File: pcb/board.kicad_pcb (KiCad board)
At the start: 4 copper layers, 159.9 x 99.9 mm, 168 parts, among them J1 Conn_02x03_Counter_Clockwise, J2 USB_B, J3 650913-5, SW1 SW_Push, U1 XC6SLX16-FTG256, U10 TPS541620, U11 74LVC1G08, U12 IS42S16100H, U13 IS42S16100H, U14 ECS-7050MV, U15 BCM56DS, U16 74LVC1G32, U17 74LS04, U18 74LS08, U19 LMC555xMM, U2 74LVC157, U3 AT25xxx, U4 TMUX1219, U5 AT25xxx, U6 74LVC1G04, U7 SN74AVC4T245PW, U8 FT2232HQ, U9 93LCxxBxxOT, Y1 12MHz

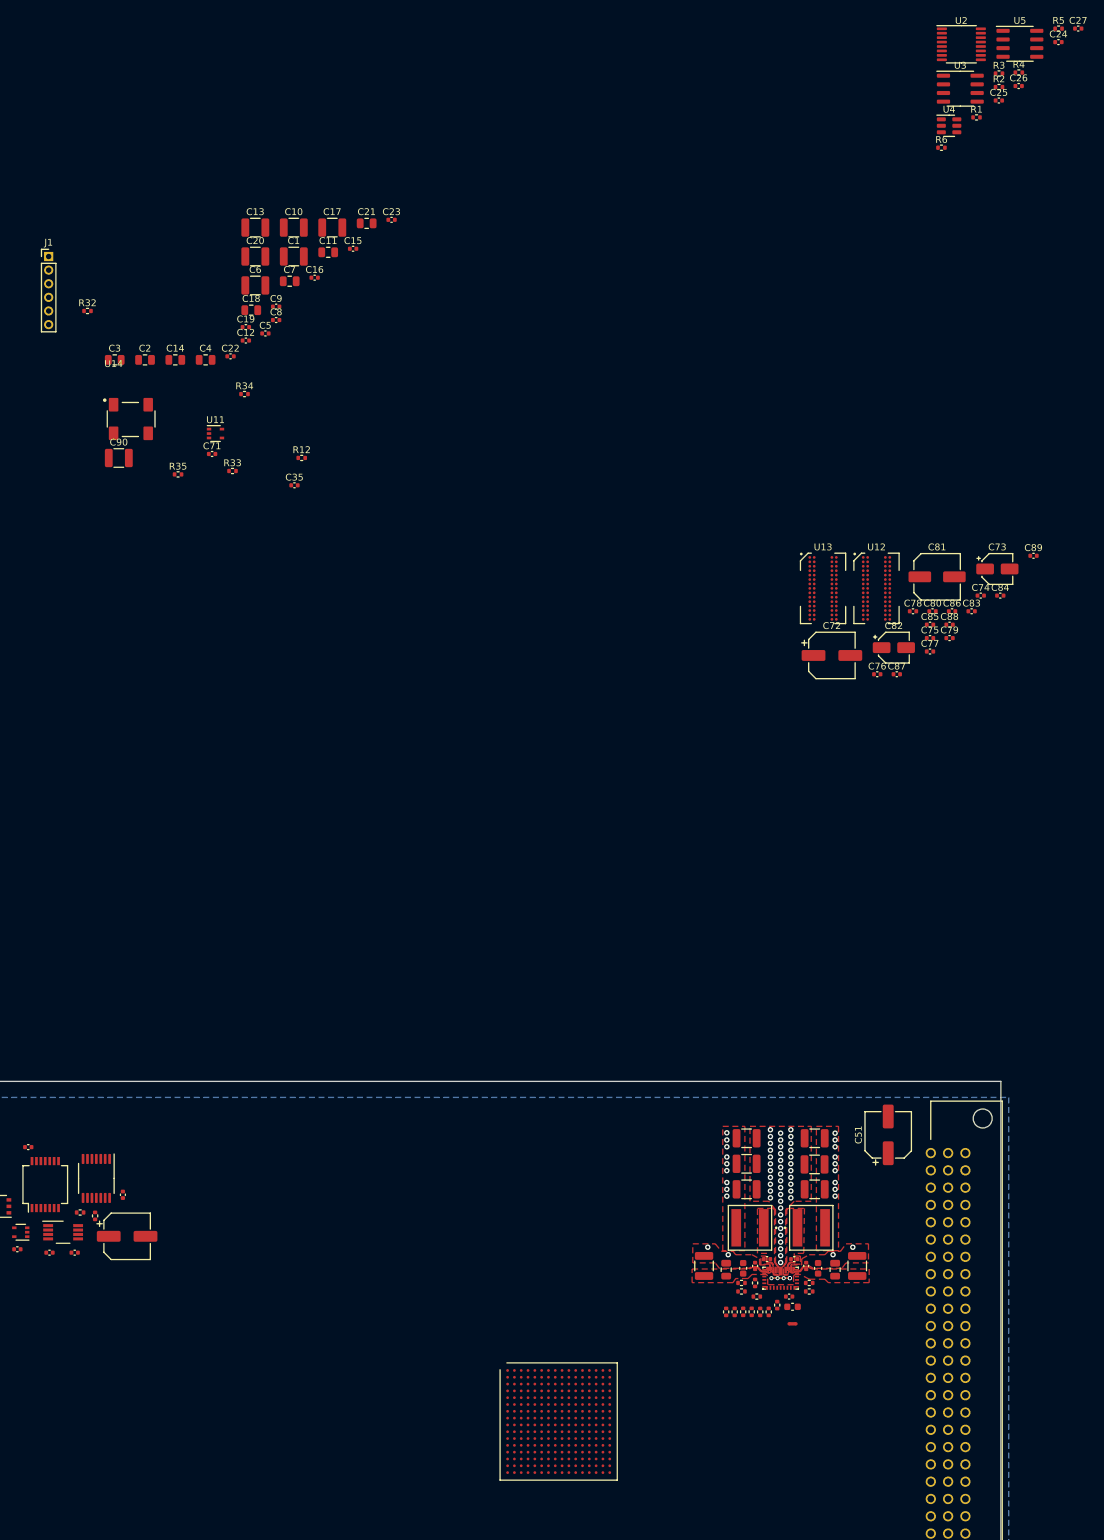
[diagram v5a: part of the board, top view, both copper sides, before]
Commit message: route pol
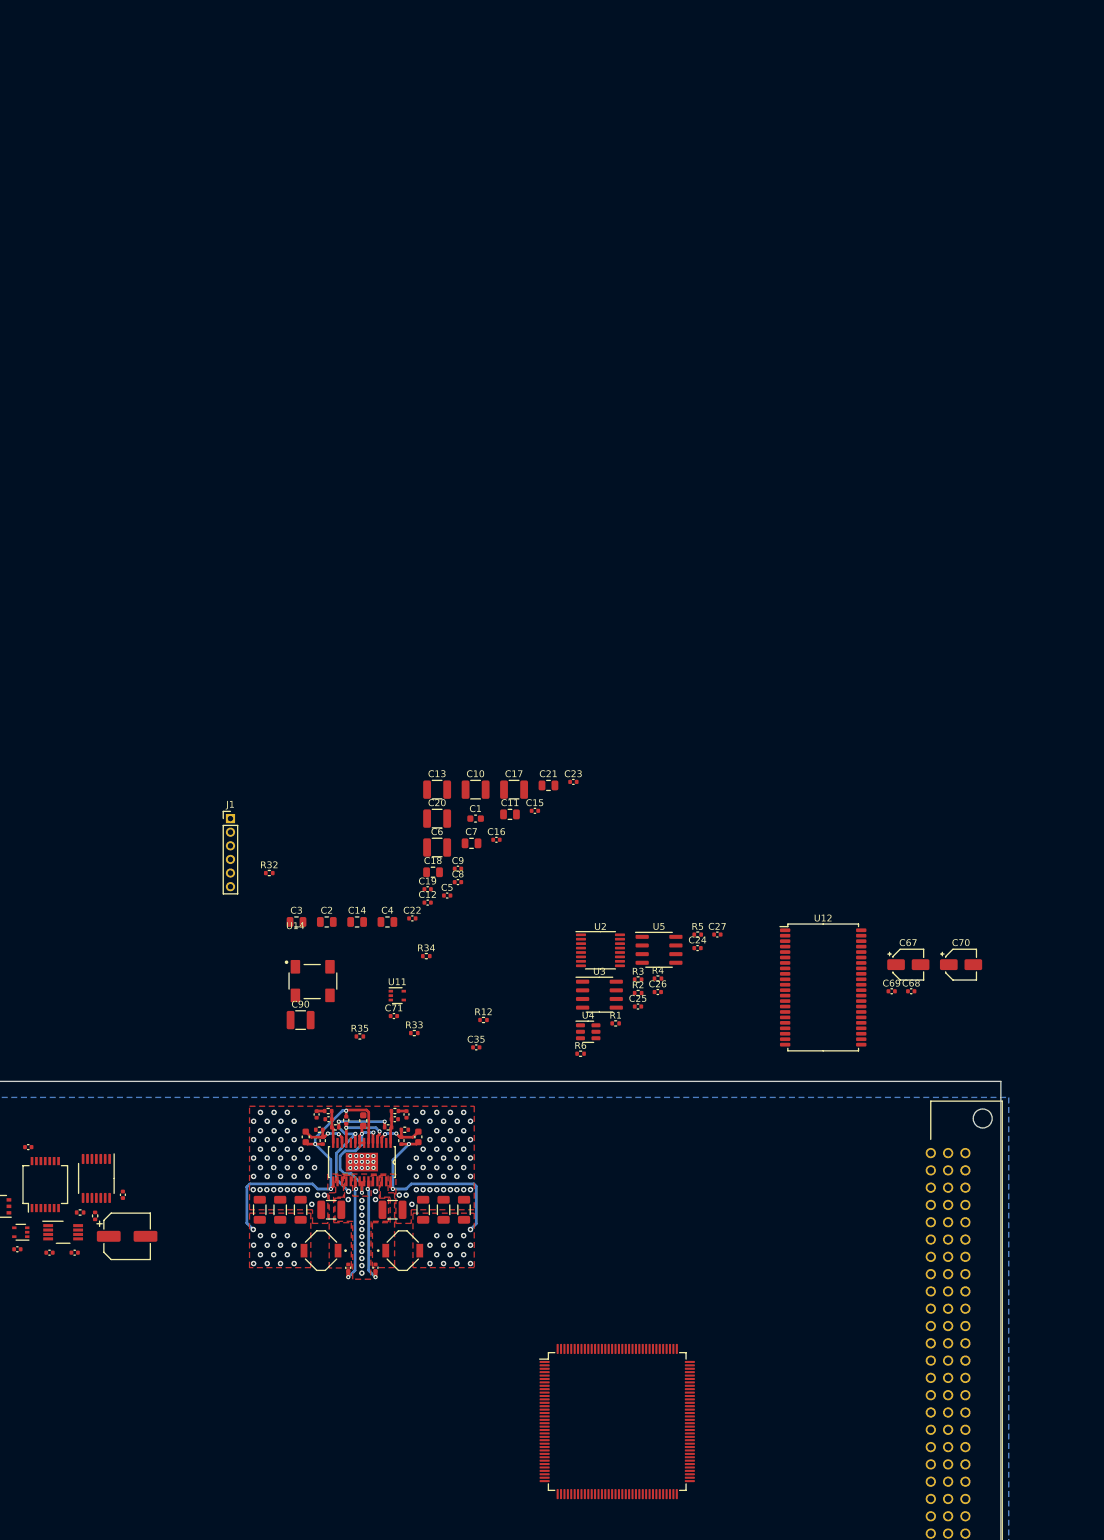
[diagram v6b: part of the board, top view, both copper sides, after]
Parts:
- removed C72: 100uF, Capacitor_SMD:CP_Elec_6.3x7.7
- removed C73, C82: 4.7uF, Capacitor_SMD:CP_Elec_4x4.5
- removed C74, C75, C76, C77, C78, C79, C80, C83, C84, C85, C86, C87, C88, C89: 470nF, Capacitor_SMD:C_0402_1005Metric
- removed C81: 100uF, Capacitor_SMD:C_Elec_6.3x7.7
- removed NT1: NetTie_2, NetTie:NetTie-2_SMD_Pad0.5mm
- removed R28: 8k, Resistor_SMD:R_0402_1005Metric
- removed R29: 39.9k, Resistor_SMD:R_0402_1005Metric
- removed R30: 15.4k, Resistor_SMD:R_0402_1005Metric
- removed R31: 17.4k, Resistor_SMD:R_0402_1005Metric
- removed U13: IS42S16100H, IS42S16100H:IS42S16100H
- added C64: 22u, Capacitor_SMD:C_1206_3216Metric, F.Cu at (109.1, 63.9)
- added C68: 0.1u, Capacitor_SMD:C_0402_1005Metric, F.Cu at (201.8, 31.8)
- C1: footprint Capacitor_SMD:C_1210_3225Metric -> Capacitor_SMD:C_0603_1608Metric
- C47: value 100uF -> 47u
- C51: value 100uF -> 47u; footprint Capacitor_SMD:CP_Elec_6.3x7.7 -> Capacitor_SMD:C_1210_3225Metric
- C52: value 47uF -> 100n; footprint Capacitor_SMD:C_1210_3225Metric -> Capacitor_SMD:C_0402_1005Metric
- C53: value 22uF -> NL; footprint Capacitor_SMD:C_0805_2012Metric -> Capacitor_SMD:C_0603_1608Metric
- C54: value 0.1uF -> 22u; footprint Capacitor_SMD:C_0603_1608Metric -> Capacitor_SMD:C_1206_3216Metric
- C55, C63: value 0.1uF -> 22u; footprint Capacitor_SMD:C_0402_1005Metric -> Capacitor_SMD:C_1206_3216Metric
- C56: value 0.1uF -> 10u; footprint Capacitor_SMD:C_0402_1005Metric -> Capacitor_SMD:C_1206_3216Metric
- C57: value 100uF -> 100n; footprint Capacitor_SMD:C_1210_3225Metric -> Capacitor_SMD:C_0402_1005Metric
- C58: value 100uF -> 10p; footprint Capacitor_SMD:C_1210_3225Metric -> Capacitor_SMD:C_0402_1005Metric
- C59: value 100uF -> 220p; footprint Capacitor_SMD:C_1210_3225Metric -> Capacitor_SMD:C_0402_1005Metric
- C60: value 47uF -> 10p; footprint Capacitor_SMD:C_1210_3225Metric -> Capacitor_SMD:C_0402_1005Metric
- C61: value 22uF -> 220p; footprint Capacitor_SMD:C_0805_2012Metric -> Capacitor_SMD:C_0402_1005Metric
- C62: value 0.1uF -> NL
- C65: value 4.7uF -> 10u; footprint Capacitor_SMD:C_0603_1608Metric -> Capacitor_SMD:C_1206_3216Metric
- C66: value 0.1uF -> 2.2uF; footprint Capacitor_SMD:C_0402_1005Metric -> Capacitor_SMD:C_0603_1608Metric
- C67: value 0.1uF -> 4.7u; footprint Capacitor_SMD:C_0402_1005Metric -> Capacitor_SMD:CP_Elec_4x4.5
- C69: value 100uF -> 0.1u; footprint Capacitor_SMD:C_1210_3225Metric -> Capacitor_SMD:C_0402_1005Metric
- C70: value 100uF -> 4.7u; footprint Capacitor_SMD:C_1210_3225Metric -> Capacitor_SMD:CP_Elec_4x4.5
- L1: value 560nH -> 1uH; footprint XAL6030-561MEB:IND_XAL6030-561MEB -> 2020_5252_Inductor:IND_#A915BY-100M=P3
- L2: value 1.2uH -> 2.2uH; footprint XAL6030-122MEB:IND_XAL6030-122MEB -> 2020_5252_Inductor:IND_#A915BY-100M=P3
- R19: value 100k -> 10k
- R20: value 14k -> 10k
- R23: value 10k -> 6.98k
- R24: value 100k -> 6.98k
- R25: value 56k -> 10k
- R26: value 10k -> 45.3k
- U1: value XC6SLX16-FTG256 -> XC6SLX9-TQG144; footprint Package_BGA:Xilinx_FTG256 -> Package_QFP:TQFP-144_20x20mm_P0.5mm
- U10: value TPS541620 -> LTC3633EFEPBF; footprint TPS541620:TPS541620 -> SOP65P640X120-29N:SOP65P640X120-29N
- U12: value IS42S16100H -> IS61WV25616EFBLL; footprint IS42S16100H:IS42S16100H -> Package_SO:TSOP-II-44_10.16x18.41mm_P0.8mm
- moved C24 143.2 mm to (170.4, 25.5)
- moved C25 143.2 mm to (161.6, 34.1)
- moved C26 143.2 mm to (164.5, 31.9)
- moved C27 143.2 mm to (173.3, 23.5)
- moved R1 143.2 mm to (158.3, 36.6)
- moved R2 143.2 mm to (161.7, 32.1)
- moved R3 143.2 mm to (161.7, 30.1)
- moved R4 143.2 mm to (164.6, 30.0)
- moved R5 143.2 mm to (170.4, 23.5)
- moved R6 143.2 mm to (153.2, 41.0)
- moved U2 143.2 mm to (156.1, 25.8)
- moved U3 143.2 mm to (156.0, 32.3)
- moved U4 143.2 mm to (154.3, 37.8)
- moved U5 143.2 mm to (164.7, 25.8)
- moved C19 86.8 mm to (130.7, 16.9)
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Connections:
- C47 pad 1: VCCAUX -> +5V
- C51 pad 1: VCC -> +5V
- C52 pad 1: VCC -> Net-(U10-Pad23)
- C52 pad 2: GND -> Net-(L1-Pad1)
- C53 pad 1: VCC -> VCCINT
- C53 pad 2: GND -> Net-(C53-Pad2)
- C54 pad 1: VCC -> VCCINT
- C55 pad 1: VCC -> VCCINT
- C56 pad 1: Net-(C56-Pad1) -> VCCINT
- C56 pad 2: Net-(C56-Pad2) -> GND
- C57 pad 1: VCCINT -> Net-(C57-Pad1)
- C57 pad 2: GND -> Net-(C57-Pad2)
- C58 pad 1: VCCINT -> Net-(C58-Pad1)
- C59 pad 1: VCCINT -> Net-(C59-Pad1)
- C60 pad 1: VCC -> Net-(C60-Pad1)
- C61 pad 1: VCC -> Net-(C61-Pad1)
- C62 pad 1: VCC -> VCCAUX
- C62 pad 2: GND -> Net-(C62-Pad2)
- C63 pad 1: VCC -> VCCAUX
- C65 pad 1: /Power Supply/BP5 -> VCCAUX
- C66 pad 1: /Power Supply/BP5 -> Net-(C66-Pad1)
- C67 pad 1: Net-(C67-Pad1) -> VCCAUX
- C67 pad 2: Net-(C67-Pad2) -> GND
- J3 pad 19: VCC -> +5V
- J3 pad 6: VCC -> +5V
- J3 pad 76: VCC -> +5V
- J3 pad 89: VCC -> +5V
- L1 pad 1: Net-(C56-Pad2) -> Net-(L1-Pad1)
- L2 pad 1: Net-(C67-Pad2) -> Net-(C57-Pad2)
- R19 pad 1: Net-(R19-Pad1) -> +5V
- R19 pad 2: /Power Supply/BP5 -> Net-(C58-Pad1)
- R20 pad 1: Net-(C64-Pad1) -> +5V
- R20 pad 2: VCCINT -> Net-(C60-Pad1)
- R21 pad 1: GND1 -> VCCAUX
- R21 pad 2: Net-(C64-Pad1) -> Net-(R21-Pad2)
- R22 pad 1: VCCAUX -> VCCINT
- R22 pad 2: /Power Supply/EN1 -> Net-(C53-Pad2)
- R23 pad 1: VCC -> Net-(C58-Pad1)
- R23 pad 2: /Power Supply/EN2 -> Net-(C59-Pad1)
- R24 pad 1: Net-(R24-Pad1) -> Net-(C60-Pad1)
- R24 pad 2: /Power Supply/BP5 -> Net-(C61-Pad1)
- R25 pad 1: Net-(C68-Pad1) -> Net-(C53-Pad2)
- R25 pad 2: VCCAUX -> GND
- R26 pad 1: Net-(R26-Pad1) -> VCCAUX
- R26 pad 2: Net-(R26-Pad2) -> Net-(C62-Pad2)
- R27 pad 1: GND1 -> Net-(C62-Pad2)
- R27 pad 2: Net-(C68-Pad1) -> GND
- U10 pad 1: Net-(C67-Pad1) -> Net-(C60-Pad1)
- U10 pad 10: Net-(R26-Pad2) -> GND
- U10 pad 11: (no net) -> Net-(R21-Pad2)
- U10 pad 12: /Power Supply/SS -> Net-(C62-Pad2)
- U10 pad 13: Net-(C64-Pad1) -> unconnected-(U10-Pad13)
- U10 pad 14: GND -> Net-(C58-Pad1)
- U10 pad 15: GND1 -> VCCAUX
- U10 pad 16: /Power Supply/BP5 -> Net-(C57-Pad2)
- U10 pad 17: Net-(C68-Pad1) -> Net-(C57-Pad2)
- U10 pad 18: /Power Supply/EN2 -> +5V
- U10 pad 19: (no net) -> +5V
- U10 pad 2: Net-(C67-Pad2) -> unconnected-(U10-Pad2)
- U10 pad 20: /Power Supply/EN1 -> Net-(C57-Pad1)
- U10 pad 21: Net-(R24-Pad1) -> Net-(C66-Pad1)
- U10 pad 22: Net-(R19-Pad1) -> Net-(C66-Pad1)
- U10 pad 23: GND -> Net-(U10-Pad23)
- U10 pad 24: VCC -> +5V
- U10 pad 25: GND -> +5V
- U10 pad 3: GND -> Net-(C53-Pad2)
- U10 pad 4: Net-(C56-Pad2) -> Net-(R21-Pad2)
- U10 pad 5: Net-(C56-Pad1) -> Net-(C66-Pad1)
- U10 pad 6: VCC -> VCCAUX
- U10 pad 7: GND -> Net-(C66-Pad1)
- U10 pad 8: /Power Supply/SYNC -> Net-(C66-Pad1)
- U10 pad 9: Net-(R26-Pad1) -> +5V
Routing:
- net VCCAUX: track 0.00 -> 46.9 mm, vias 9 -> 18
- net VCCINT: track 0.00 -> 30.9 mm, vias 9 -> 17
- net +5V: track 0.00 -> 23.8 mm, vias 0 -> 18
- net Net-(C66-Pad1): track 0.00 -> 21.8 mm, vias 0 -> 3
- net Net-(C57-Pad1): track 0.00 -> 15.5 mm, vias 0 -> 2
- net Net-(U10-Pad23): track 0.00 -> 15.5 mm, vias 0 -> 2
- net Net-(R21-Pad2): track 0.00 -> 9.76 mm, vias 0 -> 2
- net Net-(C53-Pad2): track 0.00 -> 8.08 mm, vias 0 -> 2
- net Net-(C62-Pad2): track 0.00 -> 8.03 mm, vias 0 -> 2
- net Net-(C58-Pad1): track 0.00 -> 4.77 mm
- net Net-(C60-Pad1): track 0.00 -> 4.75 mm
- net Net-(C61-Pad1): track 0.00 -> 1.20 mm
- net Net-(C59-Pad1): track 0.00 -> 1.20 mm
- net VCC: vias 4 -> 0
- net GND: vias 47 -> 107
- added copper zone on F.Cu, net +5V
- added copper zone on In2.Cu, net +5V
- added copper zone on F.Cu, net Net-(C57-Pad2)
- added copper zone on F.Cu, net Net-(L1-Pad1)
- added copper zone on In2.Cu, net VCCAUX
- added copper zone on In2.Cu, net VCCINT
- removed copper zone on F.Cu, net Net-(C56-Pad1)
- removed copper zone on F.Cu, net Net-(C56-Pad2)
- removed copper zone on F.Cu, net Net-(C67-Pad1)
- removed copper zone on F.Cu, net Net-(C67-Pad2)
- removed copper zone on F.Cu, net VCC

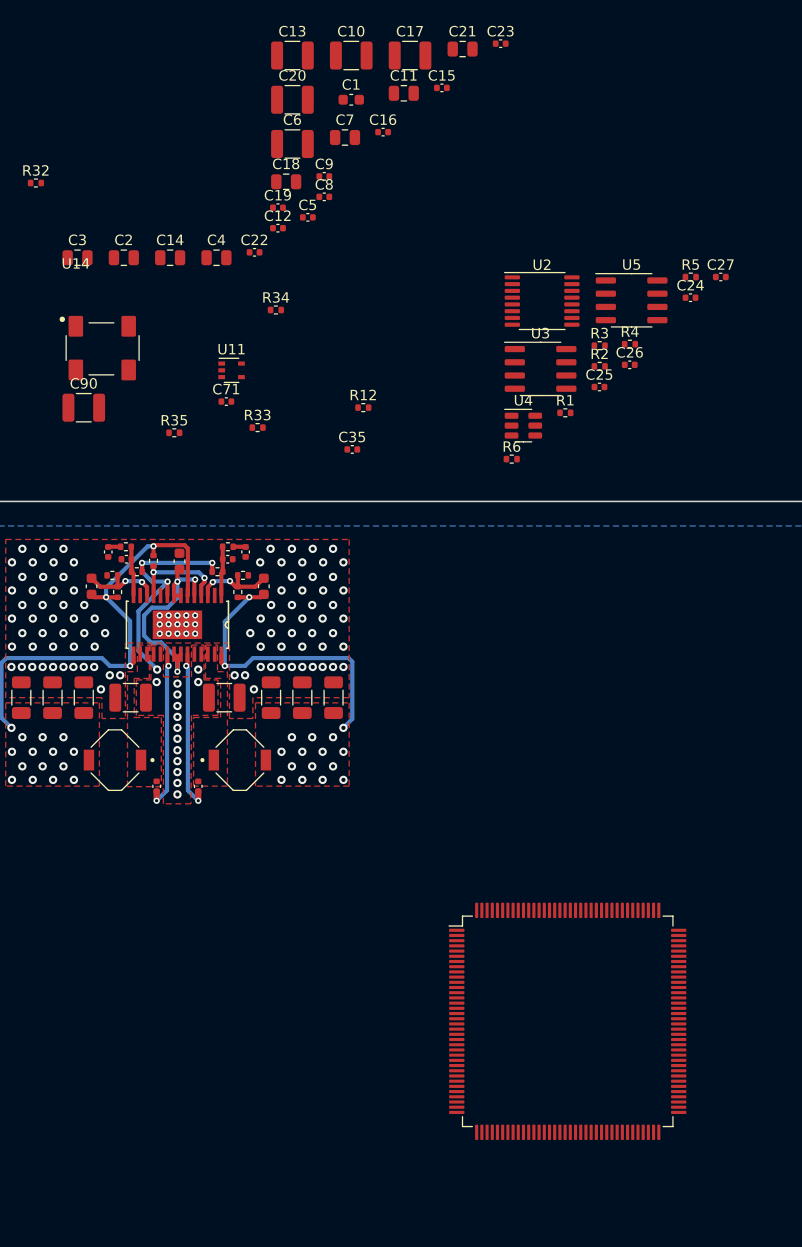
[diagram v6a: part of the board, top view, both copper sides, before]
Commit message: add decoupling caps
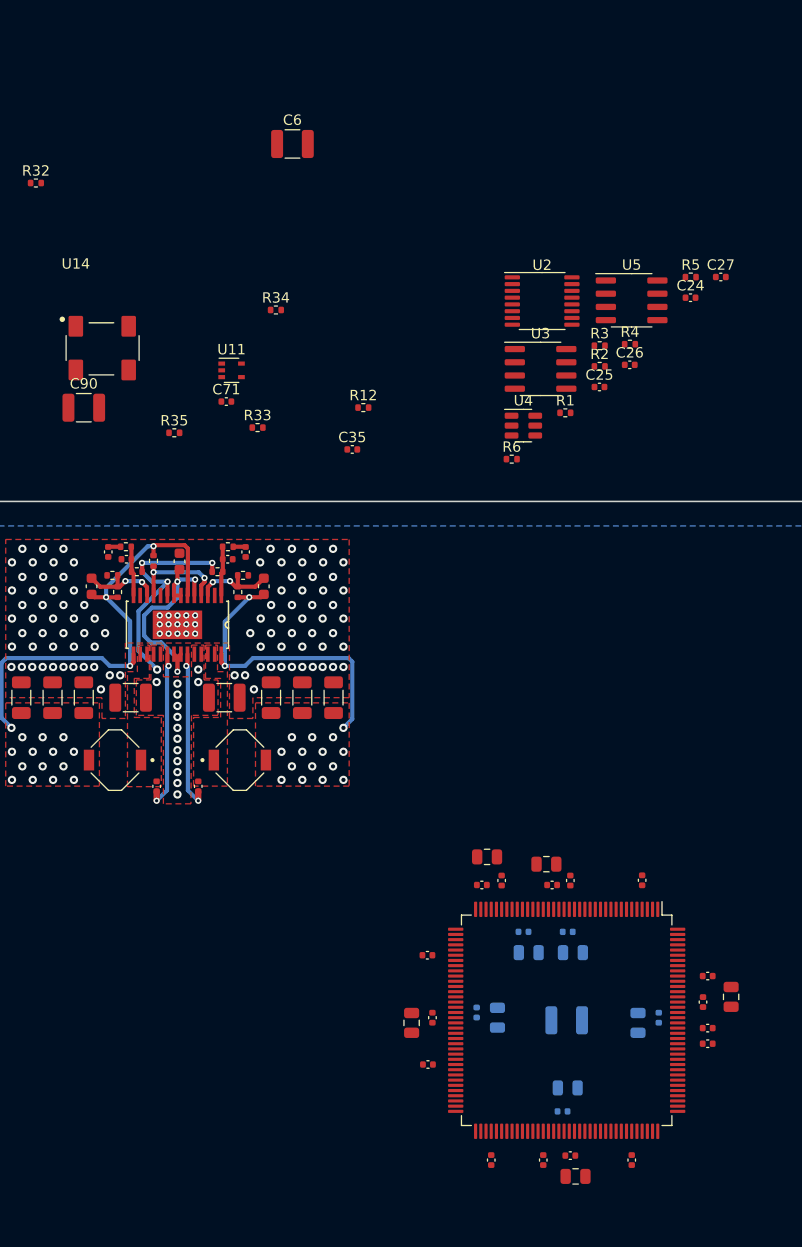
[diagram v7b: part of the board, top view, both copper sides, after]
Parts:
- removed C20: 100uF, Capacitor_SMD:C_1210_3225Metric
- removed C21: 4.7uF, Capacitor_SMD:C_0805_2012Metric
- removed C23: 470nF, Capacitor_SMD:C_0402_1005Metric
- added C72: 4.7uF, Capacitor_SMD:C_0805_2012Metric, B.Cu at (151.8, 94.7)
- added C73: 4.7uF, Capacitor_SMD:C_0805_2012Metric, B.Cu at (154.8, 88.4)
- added C74: 470nF, Capacitor_SMD:C_0402_1005Metric, B.Cu at (158.1, 103.7)
- added C75: 470nF, Capacitor_SMD:C_0402_1005Metric, B.Cu at (167.3, 94.7)
- added C76: 470nF, Capacitor_SMD:C_0402_1005Metric, B.Cu at (149.8, 94.2)
- added C77: 470nF, Capacitor_SMD:C_0402_1005Metric, B.Cu at (154.3, 86.4)
- added C78: 4.7uF, Capacitor_SMD:C_0805_2012Metric, F.Cu at (156.5, 79.9)
- added C79: 4.7uF, Capacitor_SMD:C_0805_2012Metric, F.Cu at (143.6, 95.2)
- added C80: 4.7uF, Capacitor_SMD:C_0805_2012Metric, F.Cu at (159.3, 109.9)
- added C81: 4.7uF, Capacitor_SMD:C_0805_2012Metric, F.Cu at (150.8, 79.2)
- added C82: 470nF, Capacitor_SMD:C_0402_1005Metric, F.Cu at (171.6, 93.2)
- added C83: 470nF, Capacitor_SMD:C_0402_1005Metric, F.Cu at (158.8, 107.9)
- added C84: 470nF, Capacitor_SMD:C_0402_1005Metric, F.Cu at (145.6, 94.7)
- C1: footprint Capacitor_SMD:C_0603_1608Metric -> Capacitor_SMD:C_1210_3225Metric; moved to B.Cu
- C10, C13, C17: value 100uF -> 470nF; footprint Capacitor_SMD:C_1210_3225Metric -> Capacitor_SMD:C_0402_1005Metric
- C11, C14, C18: value 4.7uF -> 470nF; footprint Capacitor_SMD:C_0805_2012Metric -> Capacitor_SMD:C_0402_1005Metric
- C2, C3, C4, C5: moved to B.Cu
- moved C13 107.8 mm to (151.2, 108.4), turned to -90 degrees
- moved C15 103.5 mm to (156.2, 108.4), turned to -90 degrees
- moved C16 101.6 mm to (164.7, 108.4), turned to -90 degrees
- moved C10 100.9 mm to (172.0, 97.2)
- moved C17 97.0 mm to (145.2, 99.2), turned to 180 degrees
- moved C3 91.1 mm to (165.3, 95.2), turned to -90 degrees
- moved C1 90.8 mm to (158.5, 94.9)
- moved C7 90.5 mm to (174.3, 92.7), turned to 90 degrees
- moved C11 89.7 mm to (172.0, 90.7)
- moved C12 87.2 mm to (172.0, 95.7)
- moved C4 86.6 mm to (158.6, 101.4)
- moved C2 79.5 mm to (159.1, 88.4)
- moved C18 75.3 mm to (165.7, 81.5), turned to 90 degrees
- moved C5 73.1 mm to (158.6, 86.4)
- moved C14 71.4 mm to (145.1, 88.7), turned to 180 degrees
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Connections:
- U1 pad 128: unconnected-(U1-Pad128) -> VCCINT
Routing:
- net Net-(C52-Pad1): vias 2 -> 1
- net (no net): vias 0 -> 1

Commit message: place all components
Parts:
- moved J1 133.5 mm to (104.1, 139.9), turned to 90 degrees
- moved C68 112.3 mm to (158.1, 135.3), turned to -90 degrees
- moved C67 111.3 mm to (145.1, 123.9), turned to 180 degrees
- moved C70 108.5 mm to (172.1, 129.9)
- moved U12 100.3 mm to (158.5, 126.9), turned to 90 degrees
- moved C27 98.7 mm to (122.4, 108.0), turned to -90 degrees
- moved C69 95.5 mm to (158.9, 118.5), turned to 90 degrees
- moved U14 88.2 mm to (137.5, 112.5), turned to -90 degrees
- moved R4 83.2 mm to (119.4, 99.9), turned to 90 degrees
- moved C24 82.6 mm to (114.7, 86.5), turned to 180 degrees
- moved R32 81.9 mm to (145.1, 87.2), turned to 180 degrees
- moved C90 81.8 mm to (129.1, 116.1), turned to 90 degrees
- moved R3 80.9 mm to (107.7, 90.3), turned to 90 degrees
- moved U2 80.8 mm to (126.1, 100.8)
- moved R5 79.8 mm to (131.1, 92.9), turned to 90 degrees
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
